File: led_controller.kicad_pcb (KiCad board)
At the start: 2 copper layers, 88.9 x 46.4 mm, 55 parts, among them J1 Screw_Terminal_01x02, J10 Conn_01x03, J2 SJ-3524-SMT, J3 Conn_01x03, J4 Conn_01x03, J5 Conn_01x03, J6 Conn_01x03, J7 Conn_01x03, J8 Conn_01x03, J9 Conn_01x03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

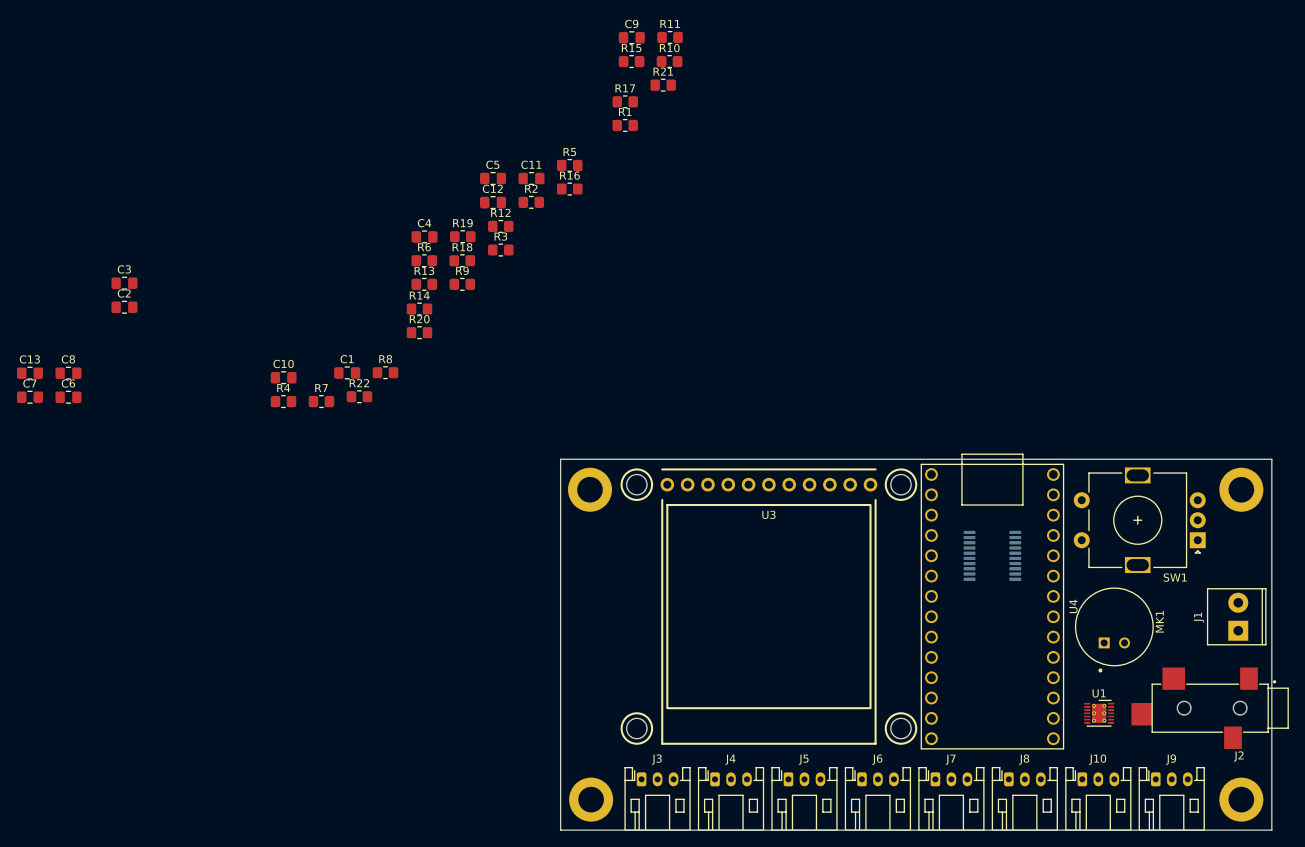
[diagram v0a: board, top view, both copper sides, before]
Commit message: Place passives, route all except power
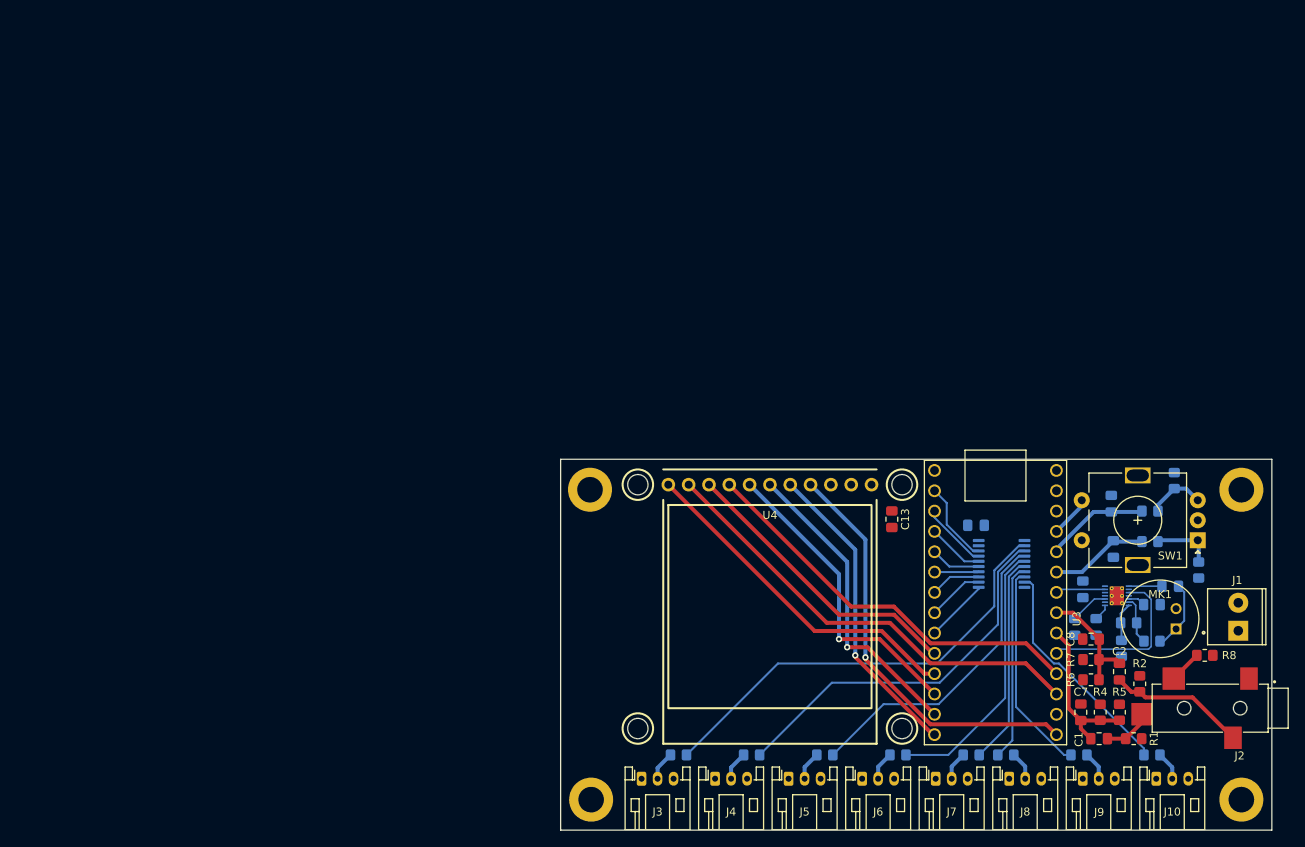
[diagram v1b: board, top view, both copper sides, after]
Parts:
- C10, C3, C4, C5, C6, C9, R10, R11, R12, R13, R14, R15, R16, R17, R18, R19, R20, R21, R22, R3, R9, U1: moved to B.Cu
- C11: value 1u -> 0.1u; moved to B.Cu
- C12: value 0.1u -> 1u; moved to B.Cu
- U3: value Adafruit_TFT_1in3_ST7789 -> Teensy4.0; footprint displays:Adafruit_TFT_1in3_ST7789 -> teensy_library:Teensy40
- U4: value Teensy4.0 -> Adafruit_TFT_1in3_ST7789; footprint teensy_library:Teensy40 -> displays:Adafruit_TFT_1in3_ST7789
- moved C7 137.1 mm to (155.2, 118.6), turned to 90 degrees
- moved C3 136.1 mm to (166.4, 102.9)
- moved C2 132.4 mm to (160.0, 113.5), turned to -90 degrees
- moved C8 132.1 mm to (156.5, 109.5), turned to 180 degrees
- moved C6 129.0 mm to (154.4, 108.0), turned to 90 degrees
- moved C13 109.3 mm to (131.6, 94.5), turned to -90 degrees
- moved R4 109.2 mm to (157.6, 118.6), turned to -90 degrees
- moved R8 108.3 mm to (170.7, 111.5), turned to 180 degrees
- moved R20 105.7 mm to (164.1, 124.0), turned to 180 degrees
- moved C10 104.6 mm to (159.0, 92.5), turned to -90 degrees
- moved C1 104.5 mm to (157.5, 121.9)
- moved R7 101.5 mm to (156.5, 112.0), turned to 180 degrees
- moved R19 100.6 mm to (155.0, 124.0), turned to 180 degrees
- moved R22 100.3 mm to (160.3, 110.6), turned to 90 degrees
- moved R1 99.6 mm to (161.8, 121.9)
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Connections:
- C1 pad 1: /AUD_R_ADC -> /AUD_L_ADC
- C1 pad 2: /AUD_R -> /AUD_L
- C11 pad 1: +3V3 -> +5V
- C12 pad 1: +5V -> +3V3
- C2 pad 1: /AUD_L_ADC -> /AUD_R_ADC
- C2 pad 2: /AUD_L -> /AUD_R
- C7 pad 1: /AUD_R_ADC -> /AUD_L_ADC
- C8 pad 1: /AUD_L_ADC -> /AUD_R_ADC
- R1 pad 1: /AUD_R -> /AUD_L
- R2 pad 1: /AUD_L -> /AUD_R
- R4 pad 2: /AUD_R_ADC -> /AUD_L_ADC
- R5 pad 1: /AUD_R_ADC -> /AUD_L_ADC
- R6 pad 2: /AUD_L_ADC -> /AUD_R_ADC
- R7 pad 1: /AUD_L_ADC -> /AUD_R_ADC
- U3 pad 1: +3V3 -> GND
- U3 pad 10: /CS_SD -> /DISP_D/C
- U3 pad 2: unconnected-(U3-Pad2) -> Net-(U2-Pad18)
- U3 pad 3: GND -> Net-(U2-Pad17)
- U3 pad 4: /SCK -> Net-(U2-Pad16)
- U3 pad 5: /MISO -> Net-(U2-Pad15)
- U3 pad 6: /MOSI -> Net-(U2-Pad14)
- U3 pad 7: /CS_TFT -> Net-(U2-Pad13)
- U3 pad 8: /DISP_RST -> Net-(U2-Pad12)
- U3 pad 9: /DISP_D/C -> Net-(U2-Pad11)
- U4 pad 1: GND -> +3V3
- U4 pad 10: /DISP_D/C -> /CS_SD
- U4 pad 11: /CS_SD -> /BACKLIGHT
- U4 pad 2: Net-(U2-Pad18) -> unconnected-(U4-Pad2)
- U4 pad 3: Net-(U2-Pad17) -> GND
- U4 pad 4: Net-(U2-Pad16) -> /SCK
- U4 pad 5: Net-(U2-Pad15) -> /MISO
- U4 pad 6: Net-(U2-Pad14) -> /MOSI
- U4 pad 7: Net-(U2-Pad13) -> /CS_TFT
- U4 pad 8: Net-(U2-Pad12) -> /DISP_RST
- U4 pad 9: Net-(U2-Pad11) -> /DISP_D/C
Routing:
- net /CS_SD: track 0.00 -> 56.8 mm
- net Net-(R13-Pad2): track 0.00 -> 55.7 mm
- net /SCK: track 0.00 -> 52.4 mm, vias 0 -> 1
- net /DISP_RST: track 0.00 -> 50.7 mm
- net Net-(R14-Pad2): track 0.00 -> 47.5 mm
- net /BACKLIGHT: track 0.00 -> 43.1 mm
- net Net-(R15-Pad2): track 0.00 -> 39.2 mm
- net /MISO: track 0.00 -> 38.8 mm, vias 0 -> 1
- net /MOSI: track 0.00 -> 38.7 mm, vias 0 -> 1
- net /CS_TFT: track 0.00 -> 38.7 mm, vias 0 -> 1
- net /DISP_D/C: track 0.00 -> 36.9 mm
- net Net-(R16-Pad2): track 0.00 -> 33.8 mm
- net Net-(R20-Pad2): track 0.00 -> 28.6 mm
- net Net-(R19-Pad2): track 0.00 -> 26.4 mm
- net Net-(R17-Pad2): track 0.00 -> 26.3 mm
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
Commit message: Rearrange screen and power, add 3D models
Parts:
- moved J1 81.1 mm to (93.7, 108.4), turned to -90 degrees
- moved C13 22.3 mm to (128.8, 116.6), turned to 90 degrees
- moved U4 21.9 mm to (131.3, 106.2), turned to -90 degrees
- moved R2 15.0 mm to (174.0, 124.7), turned to 0 degrees
- moved MK1 7.12 mm to (172.2, 107.2), turned to 180 degrees
- moved R6 6.43 mm to (155.4, 108.2), turned to -90 degrees
- moved R8 6.18 mm to (164.6, 110.5), turned to -90 degrees
- moved C11 6.12 mm to (142.6, 101.3)
- moved U2 6.12 mm to (145.8, 106.2)
- moved C7 5.86 mm to (155.7, 112.8), turned to 0 degrees
- moved R5 4.44 mm to (155.7, 117.6), turned to 0 degrees
- moved C8 4.26 mm to (160.5, 108.2), turned to 90 degrees
- moved R7 4.11 mm to (158.0, 108.2), turned to 90 degrees
- moved R4 3.92 mm to (155.7, 115.2), turned to 180 degrees
- moved R16 2.81 mm to (135.1, 124.0)
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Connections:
- U3 pad 11: /BACKLIGHT -> /DISP_RST
- U3 pad 23: /DISP_RST -> /BACKLIGHT
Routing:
- net /DISP_RST: track 50.7 -> 15.0 mm
- net /CS_SD: track 56.8 -> 29.9 mm
- net /MISO: track 38.8 -> 15.0 mm, vias 1 -> 0
- net /CS_TFT: track 38.7 -> 15.0 mm, vias 1 -> 0
- net /MOSI: track 38.7 -> 15.0 mm, vias 1 -> 0
- net /SCK: track 52.4 -> 29.7 mm, vias 1 -> 0
- net /DISP_D/C: track 36.9 -> 15.0 mm
- net /AUD_R_ADC: track 14.6 -> 0.00 mm
- net /BACKLIGHT: track 43.1 -> 29.9 mm
- net Net-(R16-Pad2): track 33.8 -> 25.2 mm
- net /AUD_L_ADC: track 19.8 -> 12.5 mm
- net Net-(U2-Pad18): track 10.2 -> 16.5 mm
- net Net-(U2-Pad17): track 8.32 -> 14.6 mm
- net Net-(R19-Pad2): track 26.4 -> 20.5 mm
- net Net-(R18-Pad2): track 24.7 -> 18.8 mm
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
